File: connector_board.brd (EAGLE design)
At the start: 55 x 25 mm, 4 parts, among them X1 0446200002

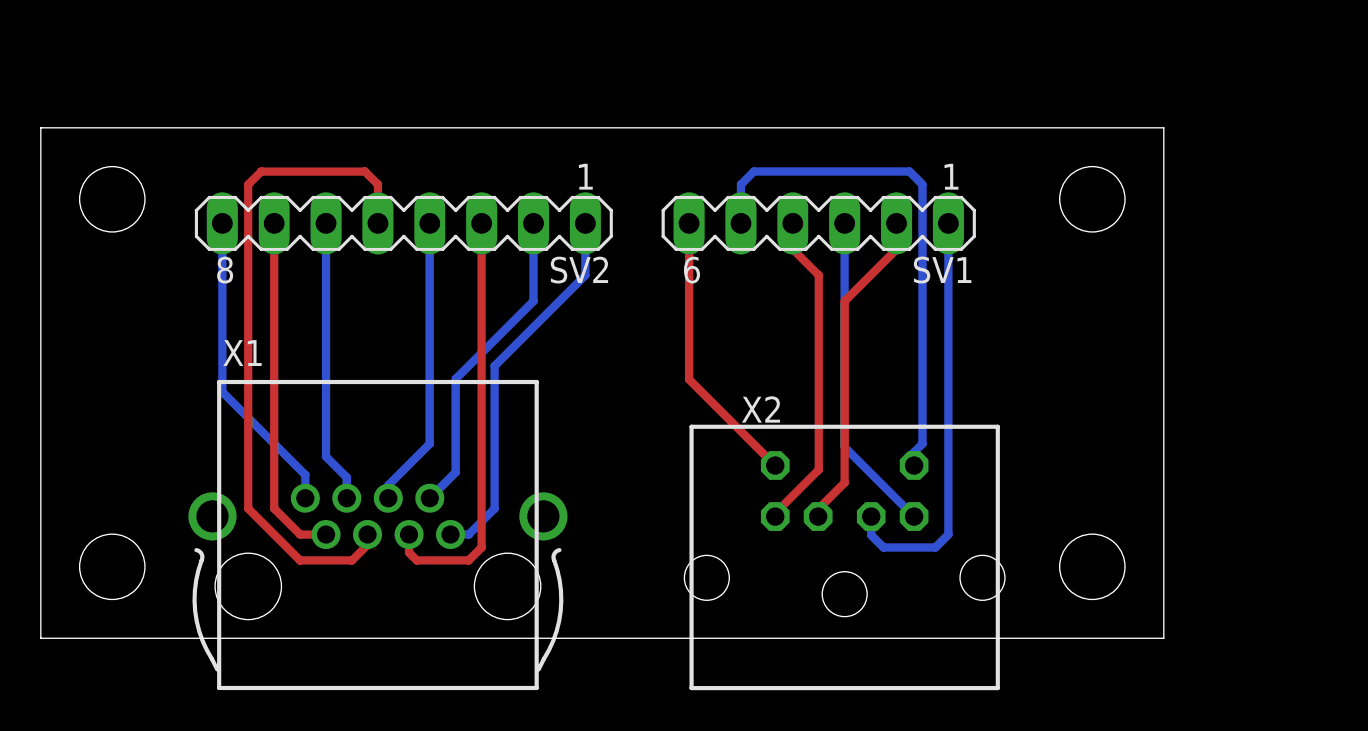
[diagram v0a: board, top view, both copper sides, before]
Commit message: added PCBs for extern IO-connections
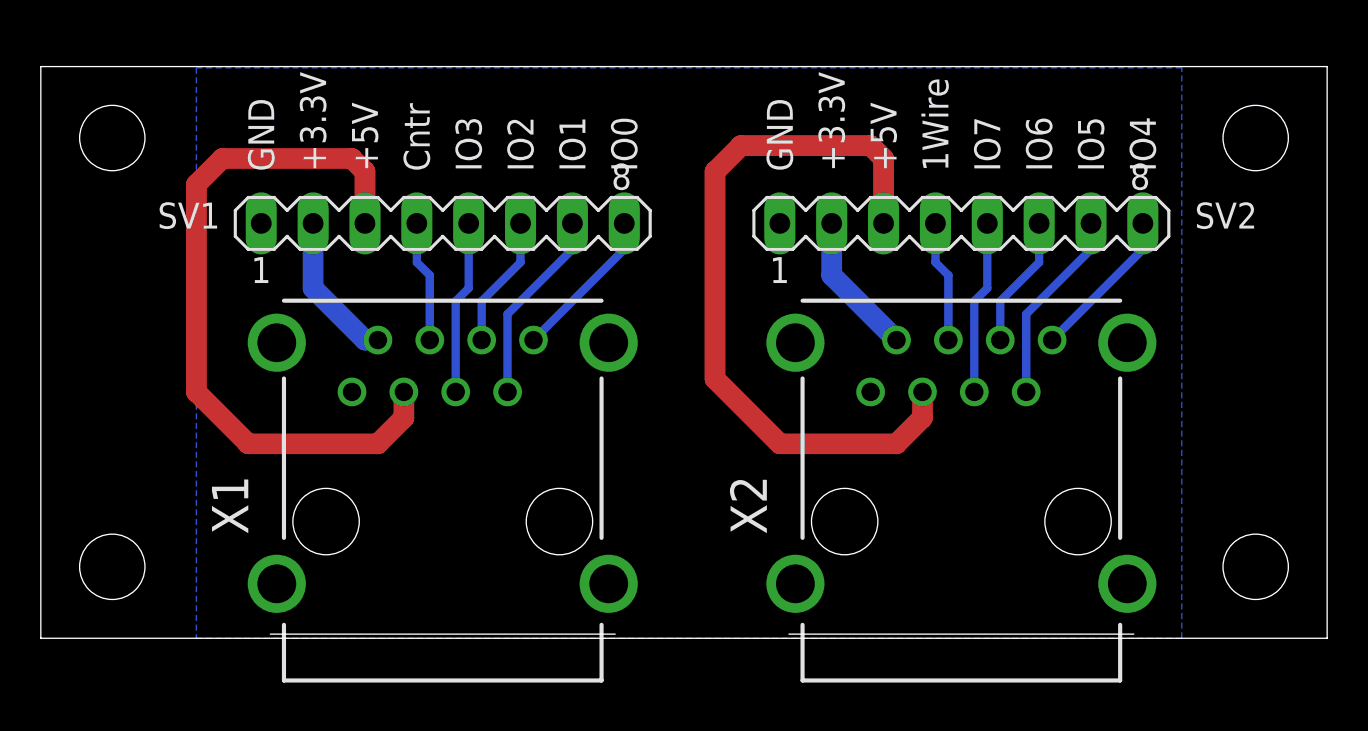
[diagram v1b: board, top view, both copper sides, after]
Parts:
- SV1: device con-lstb:MA06-1 -> con-lstb:MA08-1
- X1: value 0446200002 -> RJ45-6L21-B; device con-molex:0446200002 -> con-tycoelectronics:RJ45-SHIELD1
- X2: value (none) -> RJ45-6L21-B; device con-yamaichi:MDIN06SS -> con-tycoelectronics:RJ45-SHIELD1
- moved SV2 27.3 mm to (45.1, 20.3), turned to 0 degrees
- moved SV1 18.4 mm to (19.7, 20.3), turned to 0 degrees
- moved X2 10.0 mm to (45.1, 5.71)
- moved X1 4.49 mm to (19.7, 5.71)
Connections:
- removed net N$1: SV1.1, X2.1
- removed net N$10: SV2.4, X1.4
- removed net N$2: SV1.2, X2.2
- removed net N$9: SV2.3, X1.3
- new net GND: SV1.1, SV2.1, X1.1, X1.S1, X1.S2, X1.S3, X1.S4, X2.1, X2.S1, X2.S2, X2.S3, X2.S4
- new net N$15: SV2.7, X2.7
- new net N$16: SV2.8, X2.8
- new net N$19: SV1.2, X1.2
- new net N$20: SV2.2, X2.2
- net N$11: now also SV2.3, X2.3; no longer SV2.5, X1.5
- net N$12: now also SV2.4, X2.4; no longer SV2.6, X1.6
- net N$13: now also SV2.5, X2.5; no longer SV2.7, X1.7
- net N$14: now also SV2.6, X2.6; no longer SV2.8, X1.8
- net N$3: now also X1.3; no longer X2.3
- net N$4: now also X1.4; no longer X2.4
- net N$5: now also X1.5; no longer X2.5
- net N$6: now also X1.6; no longer X2.6
- net N$7: now also SV1.7, X1.7; no longer SV2.1, X1.1
- net N$8: now also SV1.8, X1.8; no longer SV2.2, X1.2
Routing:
- net N$9: track 20.7 -> 0.00 mm
- net N$1: track 20.4 -> 0.00 mm
- net N$3: track 15.8 -> 34.8 mm
- net N$5: track 25.3 -> 8.52 mm
- net N$2: track 16.0 -> 0.00 mm
- net N$10: track 14.3 -> 0.00 mm
- net N$4: track 15.8 -> 5.98 mm
- net N$15: track 0.00 -> 9.57 mm
- net N$7: track 18.5 -> 9.57 mm
- net N$14: track 15.1 -> 6.50 mm
- net N$13: track 17.0 -> 8.52 mm
- net N$8: track 15.6 -> 7.56 mm
- net N$12: track 13.9 -> 5.98 mm
- net N$16: track 0.00 -> 7.56 mm
- net N$19: track 0.00 -> 7.40 mm
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- added copper zone on layer 16, net GND
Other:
- board size 55 x 25 mm -> 63 x 28 mm
- board text added: "+3.3V"
- board text added: "+5V"
- board text added: "1Wire"
- board text added: "Cntr"
- board text added: "GND"
- board text added: "IO0"
- board text added: "IO1"
- board text added: "IO2"
- board text added: "IO3"
- board text added: "IO4"
- board text added: "IO5"
- board text added: "IO6"
- board text added: "IO7"
